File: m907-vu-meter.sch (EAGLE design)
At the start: 53 parts, among them U1 ERM1-5MM, U10 ERM1-5MM, U11 ERM1-5MM, U12 ERM1-5MM, U13 SCREW-M2X8, U14 SCREW-M2X8, U15 SCREW-M2X8, U16 SCREW-M2X8, U17 NUT-M2-SELFLOCK, U18 NUT-M2-SELFLOCK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

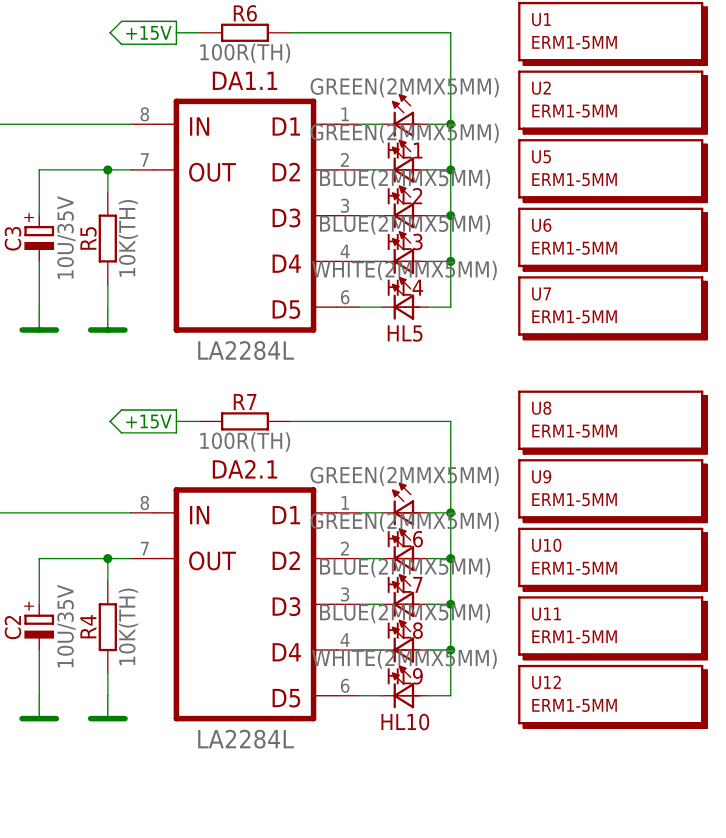
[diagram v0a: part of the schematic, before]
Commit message: M907 LED VU color update
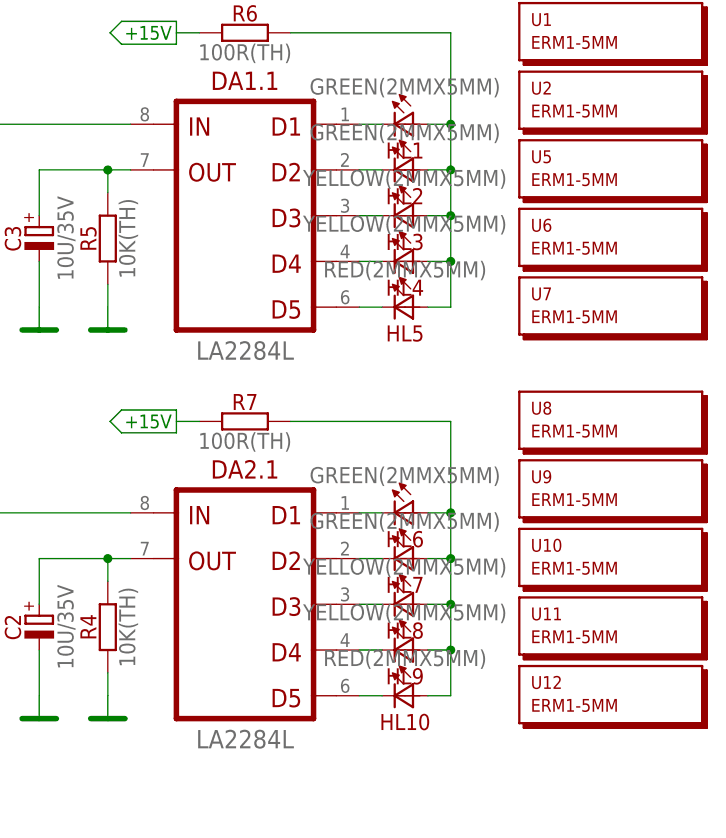
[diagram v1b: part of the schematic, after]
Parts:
- HL10, HL5: value WHITE(2MMX5MM) -> RED(2MMX5MM); device optoelectronics:WHITE(2MMX5MM) -> optoelectronics:RED(2MMX5MM)
- HL3, HL4, HL8, HL9: value BLUE(2MMX5MM) -> YELLOW(2MMX5MM); device optoelectronics:BLUE(2MMX5MM) -> optoelectronics:YELLOW(2MMX5MM)
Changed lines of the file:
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@@
 <?xml version="1.0" encoding="utf-8"?>
 <!DOCTYPE eagle SYSTEM "eagle.dtd">
-<eagle version="7.5.1">
+<eagle version="7.6.0">
 <drawing>
 <settings>
@@
 <part name="HL1" library="optoelectronics" deviceset="?(2MMX5MM)" device="GREEN"/>
 <part name="HL2" library="optoelectronics" deviceset="?(2MMX5MM)" device="GREEN"/>
-<part name="HL3" library="optoelectronics" deviceset="?(2MMX5MM)" device="BLUE"/>
-<part name="HL4" library="optoelectronics" deviceset="?(2MMX5MM)" device="BLUE"/>
-<part name="HL5" library="optoelectronics" deviceset="?(2MMX5MM)" device="WHITE"/>
+<part name="HL3" library="optoelectronics" deviceset="?(2MMX5MM)" device="YELLOW" value="YELLOW(2MMX5MM)"/>
+<part name="HL4" library="optoelectronics" deviceset="?(2MMX5MM)" device="YELLOW" value="YELLOW(2MMX5MM)"/>
+<part name="HL5" library="optoelectronics" deviceset="?(2MMX5MM)" device="RED" value="RED(2MMX5MM)"/>
 <part name="HL6" library="optoelectronics" deviceset="?(2MMX5MM)" device="GREEN"/>
 <part name="HL7" library="optoelectronics" deviceset="?(2MMX5MM)" device="GREEN"/>
-<part name="HL8" library="optoelectronics" deviceset="?(2MMX5MM)" device="BLUE"/>
-<part name="HL9" library="optoelectronics" deviceset="?(2MMX5MM)" device="BLUE"/>
-<part name="HL10" library="optoelectronics" deviceset="?(2MMX5MM)" device="WHITE"/>
+<part name="HL8" library="optoelectronics" deviceset="?(2MMX5MM)" device="YELLOW" value="YELLOW(2MMX5MM)"/>
+<part name="HL9" library="optoelectronics" deviceset="?(2MMX5MM)" device="YELLOW" value="YELLOW(2MMX5MM)"/>
+<part name="HL10" library="optoelectronics" deviceset="?(2MMX5MM)" device="RED" value="RED(2MMX5MM)"/>
 <part name="C4" library="capacitors-electrolytic" deviceset="?" device="10U/35V"/>
 <part name="C6" library="capacitors-electrolytic" deviceset="?" device="10U/35V"/>

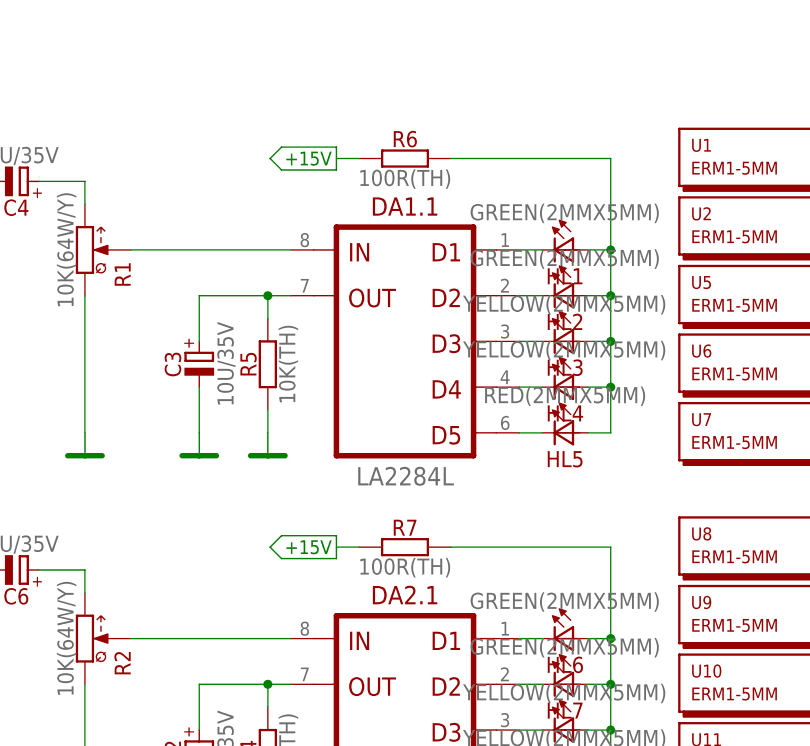
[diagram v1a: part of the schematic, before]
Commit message: M907: Change 100R to 180R
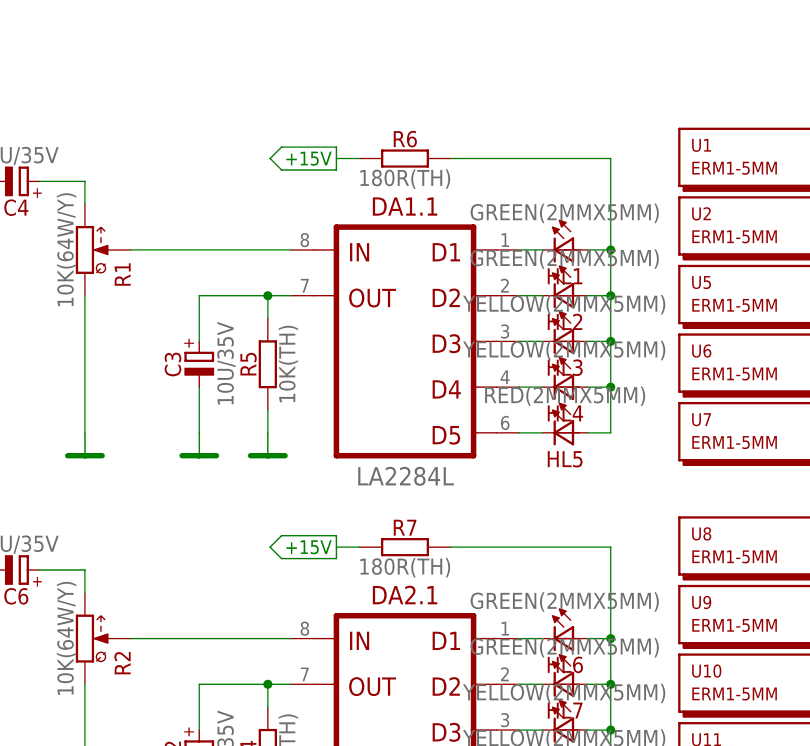
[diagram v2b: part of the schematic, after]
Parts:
- R6, R7: value 100R(TH) -> 180R(TH); device resistors:100R(TH) -> resistors:180R(TH)
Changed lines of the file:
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@@
 <part name="GND5" library="supply" deviceset="GND" device=""/>
 <part name="GND6" library="supply" deviceset="GND" device=""/>
-<part name="R6" library="resistors" deviceset="?" device="100R(TH)"/>
-<part name="R7" library="resistors" deviceset="?" device="100R(TH)"/>
+<part name="R6" library="resistors" deviceset="?" device="180R(TH)" value="180R(TH)"/>
+<part name="R7" library="resistors" deviceset="?" device="180R(TH)" value="180R(TH)"/>
 <part name="PWR1" library="supply" deviceset="+15V" device=""/>
 <part name="PWR2" library="supply" deviceset="+15V" device=""/>
